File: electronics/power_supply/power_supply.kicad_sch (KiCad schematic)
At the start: 17 parts

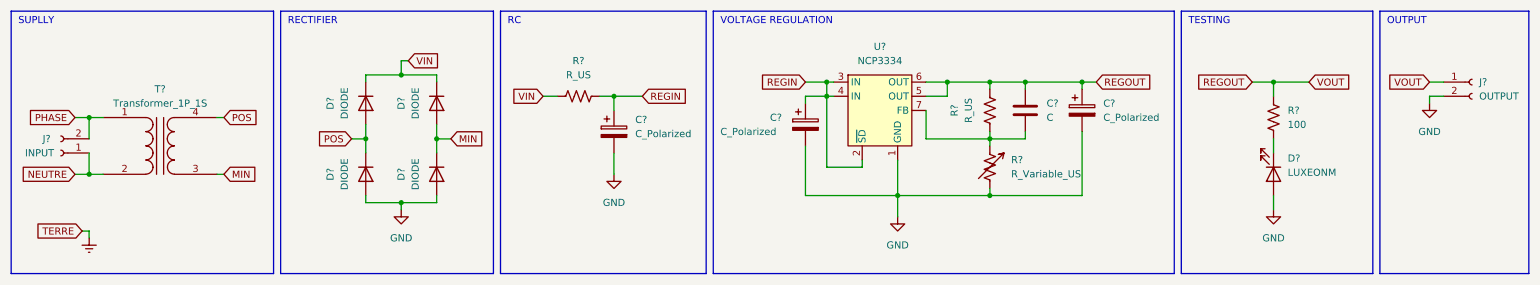
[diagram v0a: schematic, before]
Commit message: power supply pcb begin
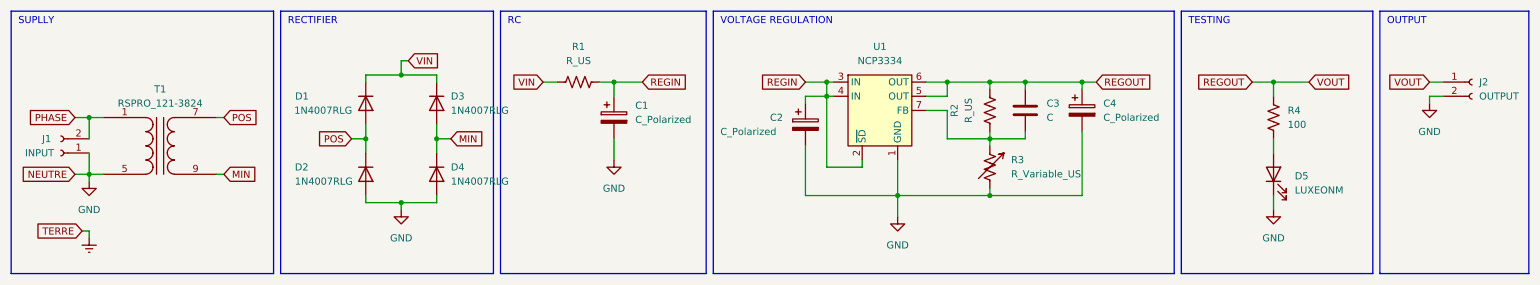
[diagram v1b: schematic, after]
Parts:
- D1, D2, D3, D4: renamed from D?; value DIODE -> 1N4007RLG; footprint (none) -> Diode_THT:D_DO-41_SOD81_P7.62mm_Horizontal
- J1: renamed from J?; footprint (none) -> USER:bornier_1x2_p5.00mm
- T1: renamed from T?; value Transformer_1P_1S -> RSPRO_121-3824; footprint (none) -> Transformer_THT:RSRO_121-3824
- gave numbers to parts that had none: 11
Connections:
- net GND: now also D2.2 (A), D4.2 (A), D5.1 (K), J1.1 (Pin_1), T1.5 (AB); no longer D2.1 (A), D4.1 (A), D5.2 (A)
- net MIN: now also D3.2 (A), D4.1 (K), T1.9 (SA); no longer D3.1 (A), D4.2 (K), T1.3 (SA)
- net POS: now also D1.2 (A), D2.1 (K), T1.7; no longer D1.1 (A), D2.2 (K), T1.4 (SB)
- net VIN: now also D1.1 (K), D3.1 (K); no longer D1.2 (K), D3.2 (K)
- net at R4.1: now also D5.2 (A); no longer D5.1 (K)
- removed net NEUTRE: J1.1 (Pin_1), T1.2 (AB)
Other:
- moved on the sheet: C1, D5, R1

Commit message: RC low pass design for power_supply
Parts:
- removed C1: C_Polarized, symbol Device:C_Polarized
- removed R1: R_US, symbol Device:R_US
- added C?: 470u, symbol Device:C
- added R?: 130, symbol Device:R_US
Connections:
- net GND: now also C?.1
- net REGIN: now also C?.2, R?.1
- net VIN: now also R?.2
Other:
- note added: "RC HIGH PASS FILTER"
- note removed: "RC"
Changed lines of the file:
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@@
     (effects (font (size 1.27 1.27)) (justify left bottom))
   )
-  (text "RC" (at 101.6 15.24 0)
+  (text "RC HIGH PASS FILTER" (at 101.6 15.24 0)
     (effects (font (size 1.27 1.27)) (justify left bottom))
   )
@@
     (pin "1")
     (pin "5")
+    (pin "7")
     (pin "9")
-    (pin "7")
-  )
-  (symbol (lib_id "Device:R_US") (at 114.3 25.4 90) (unit 1)
-    (in_bom yes) (on_board yes) (fields_autoplaced)
-    (property "Reference" "R1" (id 0) (at 114.3 19.05 90))
-    (property "Value" "R_US" (id 1) (at 114.3 21.59 90))
-    (property "Footprint" "" (id 2) (at 114.554 24.384 90)
-      (effects (font (size 1.27 1.27)) hide)
-    )
-    (property "Datasheet" "~" (id 3) (at 114.3 25.4 0)
-      (effects (font (size 1.27 1.27)) hide)
-    )
-    (pin "1")
-    (pin "2")
   )
   (symbol (lib_id "Device:LED") (at 238.76 41.91 90) (unit 1)
@@
       (effects (font (size 1.27 1.27)) (justify left) hide)
     )
-    (pin "2")
-    (pin "1")
+    (pin "1")
+    (pin "2")
   )
   (symbol (lib_id "Device:C_Polarized") (at 154.94 33.02 0) (unit 1)
@@
     (pin "2")
   )
-  (symbol (lib_id "Device:C_Polarized") (at 120.65 31.75 0) (unit 1)
-    (in_bom yes) (on_board yes) (fields_autoplaced)
-    (property "Reference" "C1" (id 0) (at 124.46 29.5909 0)
-      (effects (font (size 1.27 1.27)) (justify left))
-    )
-    (property "Value" "C_Polarized" (id 1) (at 124.46 32.1309 0)
-      (effects (font (size 1.27 1.27)) (justify left))
-    )
-    (property "Footprint" "" (id 2) (at 121.6152 35.56 0)
+  (symbol (lib_id "Device:C") (at 120.65 31.75 180) (unit 1)
+    (in_bom yes) (on_board yes) (fields_autoplaced)
+    (property "Reference" "C?" (id 0) (at 124.46 30.4799 0)
+      (effects (font (size 1.27 1.27)) (justify right))
+    )
+    (property "Value" "470u" (id 1) (at 124.46 33.0199 0)
+      (effects (font (size 1.27 1.27)) (justify right))
+    )
+    (property "Footprint" "" (id 2) (at 119.6848 27.94 0)
       (effects (font (size 1.27 1.27)) hide)
     )
     (property "Datasheet" "~" (id 3) (at 120.65 31.75 0)
+      (effects (font (size 1.27 1.27)) hide)
+    )
+    (pin "1")
+    (pin "2")
+  )
+  (symbol (lib_id "Device:R_US") (at 114.3 25.4 270) (unit 1)
+    (in_bom yes) (on_board yes) (fields_autoplaced)
+    (property "Reference" "R?" (id 0) (at 114.3 19.05 90))
+    (property "Value" "130" (id 1) (at 114.3 21.59 90))
+    (property "Footprint" "" (id 2) (at 114.046 26.416 90)
+      (effects (font (size 1.27 1.27)) hide)
+    )
+    (property "Datasheet" "~" (id 3) (at 114.3 25.4 0)
       (effects (font (size 1.27 1.27)) hide)
     )
@@
       (reference "#PWR0107") (unit 1) (value "GND") (footprint "")
     )
-    (path "/f0e88ca5-cfe1-4efd-9e98-3add5947a49b"
-      (reference "C1") (unit 1) (value "C_Polarized") (footprint "")
-    )
     (path "/4f09f720-7334-4ff5-aec1-8502d26477ac"
       (reference "C2") (unit 1) (value "C_Polarized") (footprint "")
@@
       (reference "C4") (unit 1) (value "C_Polarized") (footprint "")
     )
+    (path "/f04ce009-5053-44fb-a5cc-2b9080d20ae1"
+      (reference "C?") (unit 1) (value "470u") (footprint "")
+    )
     (path "/ff297566-3374-450d-a00f-69cf32543b39"
       (reference "D1") (unit 1) (value "1N4007RLG") (footprint "Diode_THT:D_DO-41_SOD81_P7.62mm_Horizontal")
@@
       (reference "J2") (unit 1) (value "OUTPUT") (footprint "")
     )
-    (path "/1b949c5b-9c4c-45e5-a8b0-54be38989e70"
-      (reference "R1") (unit 1) (value "R_US") (footprint "")
-    )
     (path "/0fb0fa52-9f2d-4479-8f9e-abddf31e8ada"
       (reference "R2") (unit 1) (value "R_US") (footprint "")
@@
       (reference "R4") (unit 1) (value "100") (footprint "")
     )
+    (path "/f1f0be2d-ebca-4268-a401-690830272c32"
+      (reference "R?") (unit 1) (value "130") (footprint "")
+    )
     (path "/12060b7b-d07f-47b0-ad31-dc5b5031aa34"
